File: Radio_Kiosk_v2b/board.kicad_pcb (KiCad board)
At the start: 2 copper layers, 84 x 141 mm, 239 parts, among them J1 USB-C PD in, J11 UART, J12 USB-C, J13 Lid LEDs, J2 DC in 18-26V, PJ-002BH 5.5x2.5, J3 Laptop out 15.6V, PJ-002BH 5.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, J5 RJ45 radio, J6 RJ45 laptop, J8 Fan 12V, J9 SWD, Q1 SI4470EY, Q10 2N7002, Q11 AO3400A, Q12 SI4470EY, Q13 AO4482, Q2 SI4470EY, Q20 AO4482, Q22 PSMN075-100MSEX, Q23 DMP10H400SE, Q24 BSS123, Q25 2N7002, Q30 AO3400A, Q40 AOD4184A, Q41 AOD4184A, Q44 SI4401DDY, Q45 2N7002, Q6 SI4470EY, Q7 SI4470EY, Q8 AOD4185, Q9 2N7002, SW1 RESET, SW2 BOOT0 (DFU), U1 LM74700-Q1, U10 TLV7011, U12 LM74700-Q1, U2 LM74700-Q1, U20 LM3478 54V boost, U21 TPS26600 eFuse, U22 LTC4279, U3 LMR33630 12V, U30 SN74AHCT1G125, U31 SN74AHCT1G125, U4 LM3150 15.75V 4.5A, U40 STM32F072CBT6, U41 INA180A1, U42 INA180A1, U43 MCP6001T-I/OT, U45 TLV7011, U5 LMR33630 5V, U50 CH224A, U51 AP2112K-3.3, U52 USBLC6-2SC6, U6 LM74700-Q1, U7 LM74700-Q1

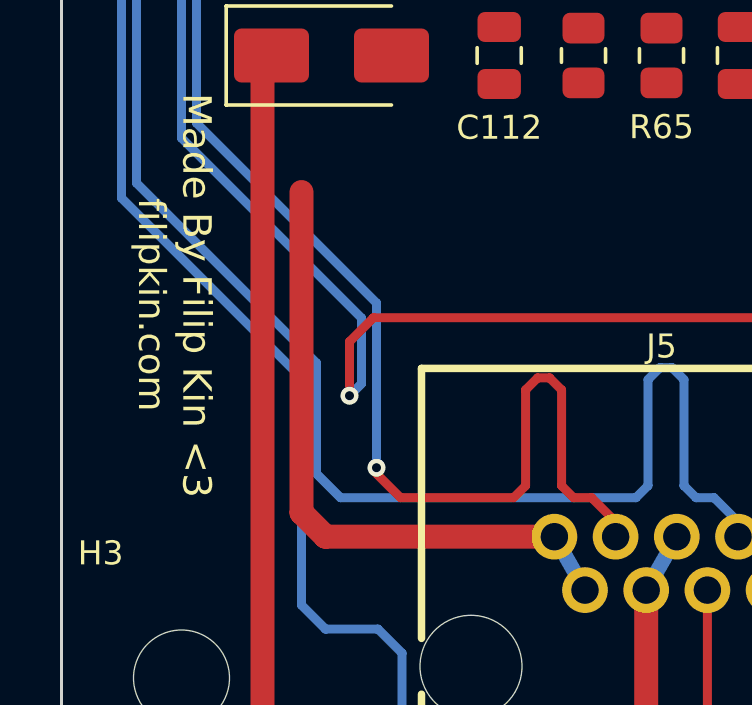
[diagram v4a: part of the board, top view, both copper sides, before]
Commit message: v2b: dead PORT_N lead at J5 removed (it ran to D22, which is now PORT_P to GND)
Co-Authored-By: Claude Opus 5.5 (1M context) <noreply@anthropic.com>
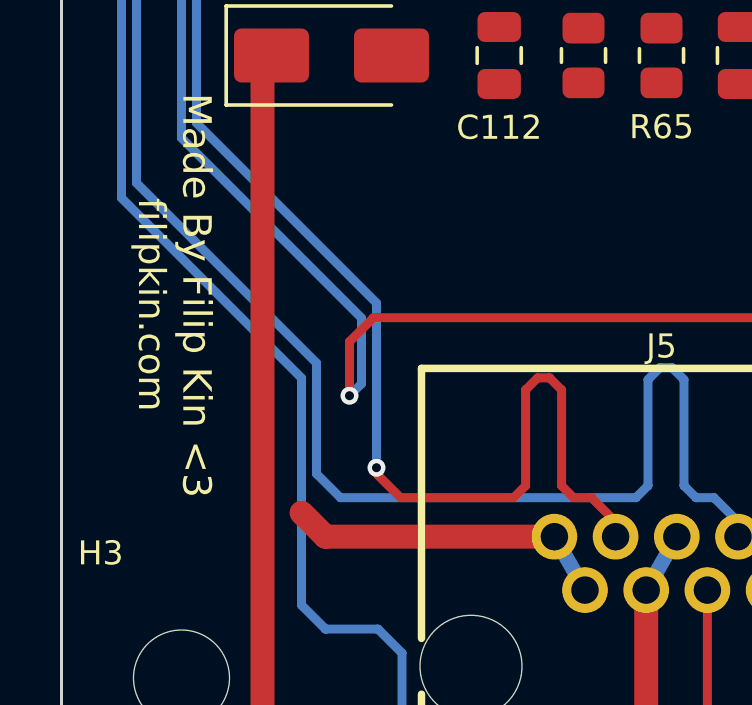
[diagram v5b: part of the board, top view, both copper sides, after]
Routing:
- net PORT_N: track 21.5 -> 10.8 mm
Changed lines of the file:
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@@
-	)
-	(segment
-		(start 8 131.49)
-		(end 8 120.8)
-		(width 0.8)
-		(layer "F.Cu")
-		(net "PORT_N")
 	)
 	(segment

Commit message: v2b: PORT_N and BK_ARM tails left by the earlier removals taken out
Co-Authored-By: Claude Opus 5.5 (1M context) <noreply@anthropic.com>
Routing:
- net PORT_N: track 10.8 -> 2.05 mm
- net BK_ARM: track 1.49 -> 0.00 mm
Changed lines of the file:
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@@
-	)
-	(segment
-		(start 8.8 132.29)
-		(end 8 131.49)
-		(width 0.8)
-		(layer "F.Cu")
-		(net "PORT_N")
-	)
-	(segment
-		(start 16.43 132.29)
-		(end 8.8 132.29)
-		(width 0.8)
-		(layer "F.Cu")
-		(net "PORT_N")
 	)
 	(segment
@@
 		(net "PORT_N")
 	)
-	(segment
-		(start 32.392 53.95)
-		(end 33.444 55.002)
-		(width 0.4)
-		(layer "F.Cu")
-		(net "BK_ARM")
-	)
 	(zone

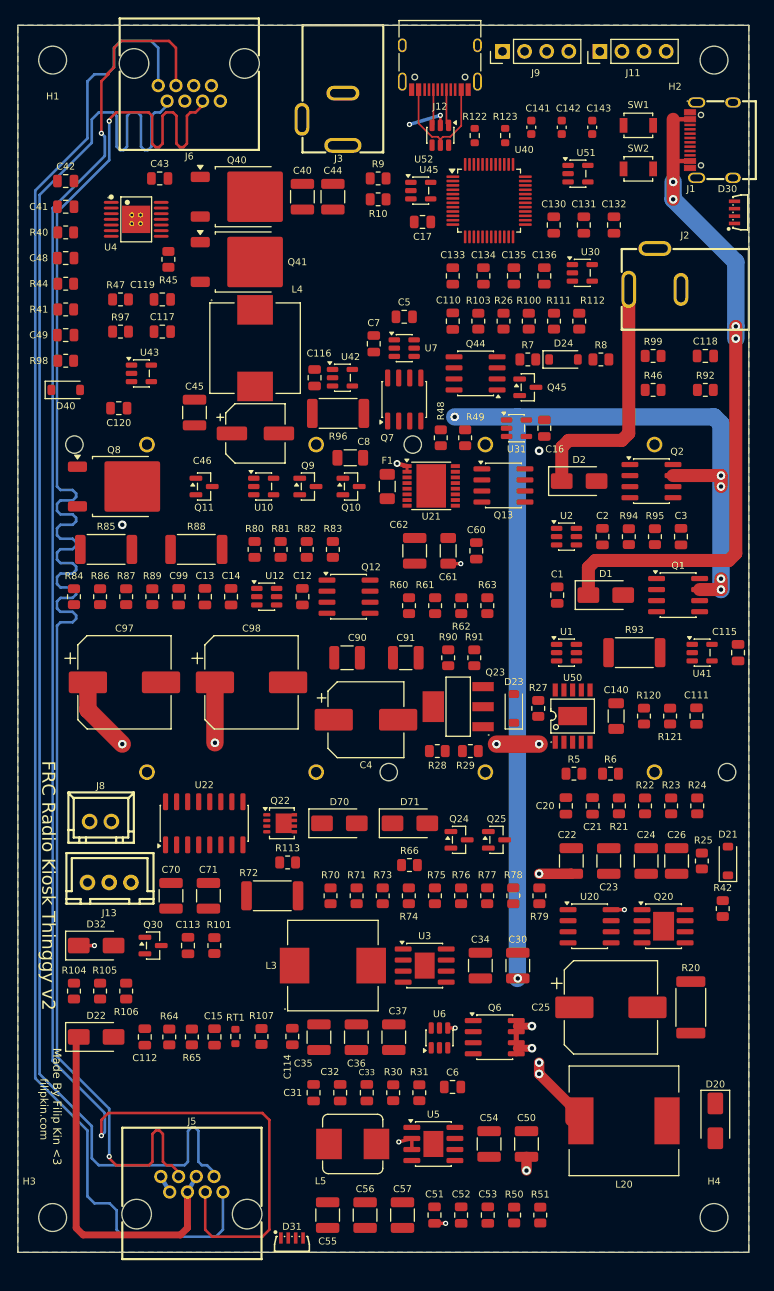
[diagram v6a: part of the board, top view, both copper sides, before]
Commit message: v2b: Filip's hand routing, moved to 1 oz copper
Filip's KiCad routing (1013 segments) taken in, then:
- net classes for 1 oz at ~20 C rise: Heavy 2.0, Wide 1.6, Power 0.8;
  duplicate Power pattern on +15V6_S removed, PORT_SW_G back to Default
- 199 power segments widened to the new class width where they clear
  every other-net pad, track, via, hole (0.25) and the edge; one VIN_USB
  run kept at 1.5 because widening cut D1's ground off
- 50 vias added beside single vias on full-width power runs
  (Heavy/Wide 3, Power 2)
- GND jumpers (via pair + back segment) join three cut-off front GND
  regions (R83, C130, U40.8); R65's region has no room and stays open
- removed: PORT_N run 0.06 mm from ETH_6 at J5, USB_VBUS via crowding
  CC1/CC2 at J12, 5 dangling vias, 1 dangling stub
Ethernet copper identical to the approved routing. DRC errors: only J1's
own 0.10 mm pad gaps.

Co-Authored-By: Claude Opus 5.5 (1M context) <noreply@anthropic.com>
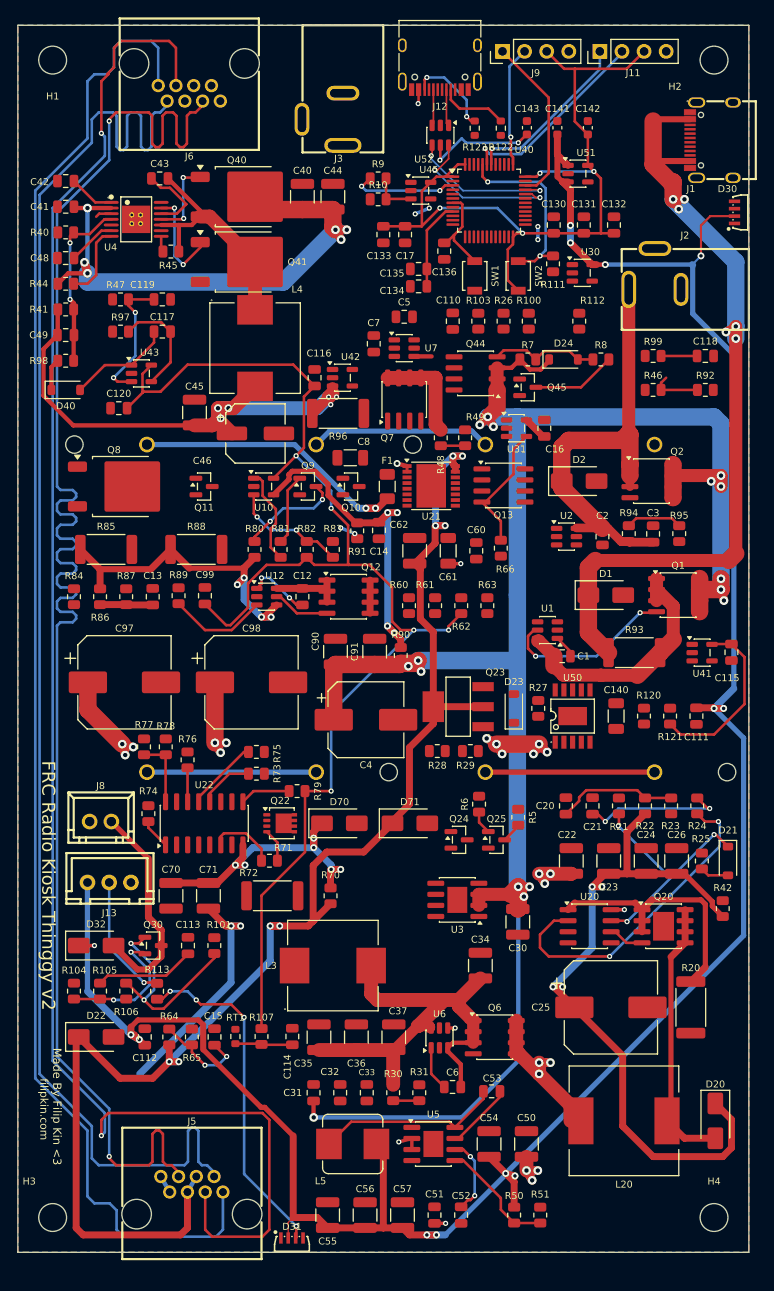
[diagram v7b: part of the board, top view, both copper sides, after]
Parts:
- moved R78 43.4 mm to (17.0, 82.9)
- moved R77 43.0 mm to (14.5, 82.9), turned to -90 degrees
- moved R66 37.9 mm to (55.5, 60.1), turned to -90 degrees
- moved R76 35.1 mm to (19.5, 84.4)
- moved R74 31.4 mm to (15.0, 90.6)
- moved R79 30.3 mm to (32.1, 88.0), turned to 180 degrees
- moved R75 26.3 mm to (27.4, 83.5), turned to 0 degrees
- moved SW1 25.5 mm to (52.5, 28.8), turned to -90 degrees
- moved R113 21.1 mm to (16.0, 111.0), turned to 90 degrees
- moved R73 20.2 mm to (27.4, 86.0), turned to 0 degrees
- moved R91 19.8 mm to (39.0, 58.1), turned to -90 degrees
- moved C14 18.6 mm to (41.5, 58.0), turned to -90 degrees
- moved SW2 18.5 mm to (57.5, 28.8), turned to -90 degrees
- moved R6 15.5 mm to (53.0, 89.5), turned to 90 degrees
- moved C53 14.2 mm to (54.5, 122.5), turned to 180 degrees
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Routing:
- net +5V: track 0.00 -> 279.9 mm, vias 0 -> 12
- net +3V3: track 0.00 -> 262.9 mm, vias 0 -> 9
- net VIN: track 125.0 -> 304.5 mm, vias 6 -> 22
- net PORT_P: track 41.8 -> 165.9 mm, vias 0 -> 8
- net BOOST_OUT: track 0.00 -> 83.1 mm, vias 0 -> 4
- net +15V6_BUCK: track 0.00 -> 66.8 mm, vias 0 -> 6
- net +12V_BUCK: track 0.00 -> 53.4 mm
- net BK_MID: track 0.00 -> 42.5 mm, vias 0 -> 4
- net LED_D2: track 0.00 -> 39.5 mm, vias 0 -> 4
- net VIN_SENSE: track 0.00 -> 38.9 mm, vias 0 -> 4
- net BOOST_COMP: track 0.00 -> 37.4 mm, vias 0 -> 2
- net PSE_AGND: track 0.00 -> 36.0 mm, vias 0 -> 6
- net +12V: track 53.0 -> 86.8 mm, vias 19 -> 28
- net PACK_P: track 0.00 -> 33.3 mm, vias 0 -> 2
- net BOOST_SW: track 0.00 -> 31.5 mm
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
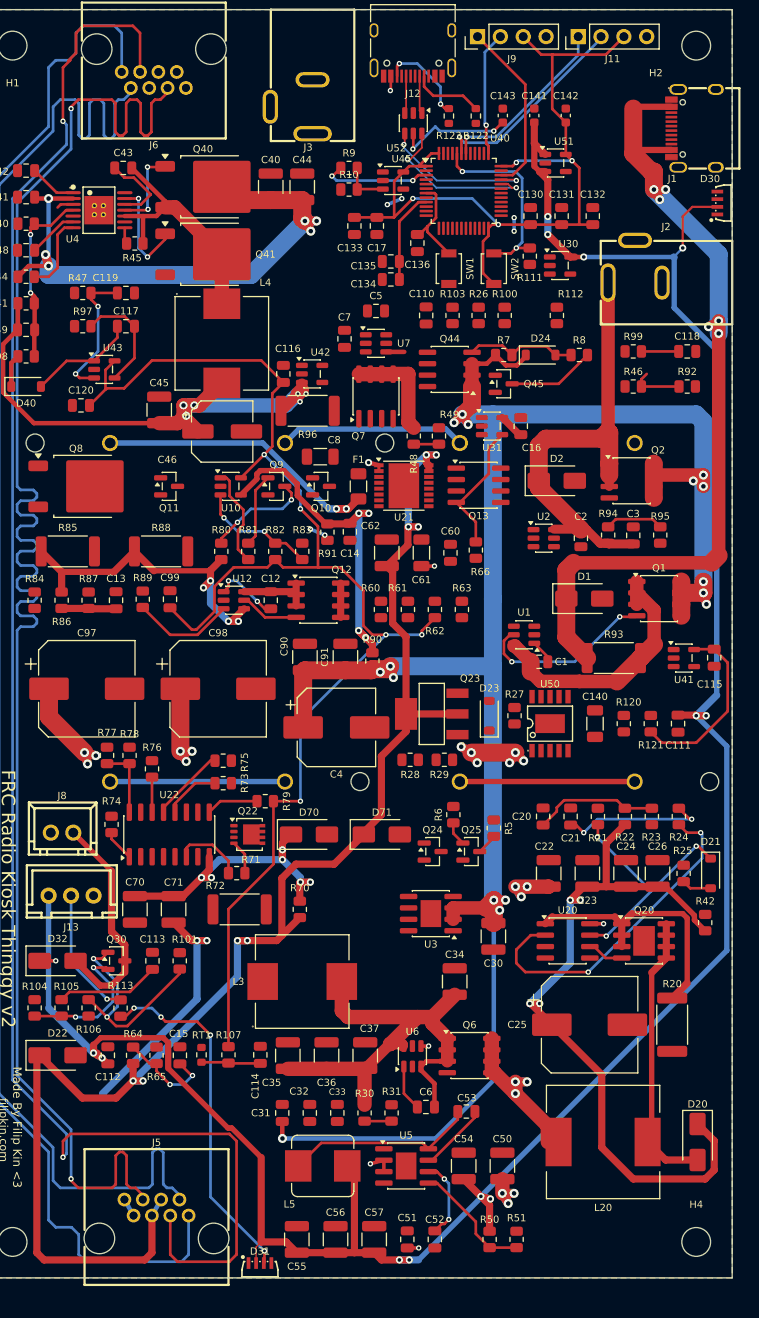
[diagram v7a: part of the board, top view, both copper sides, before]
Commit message: v2b: Filip's routing pass 2 (U3 caps moved in, PORT_N, PD lines, LED chain)
Co-Authored-By: Claude Opus 5.5 (1M context) <noreply@anthropic.com>
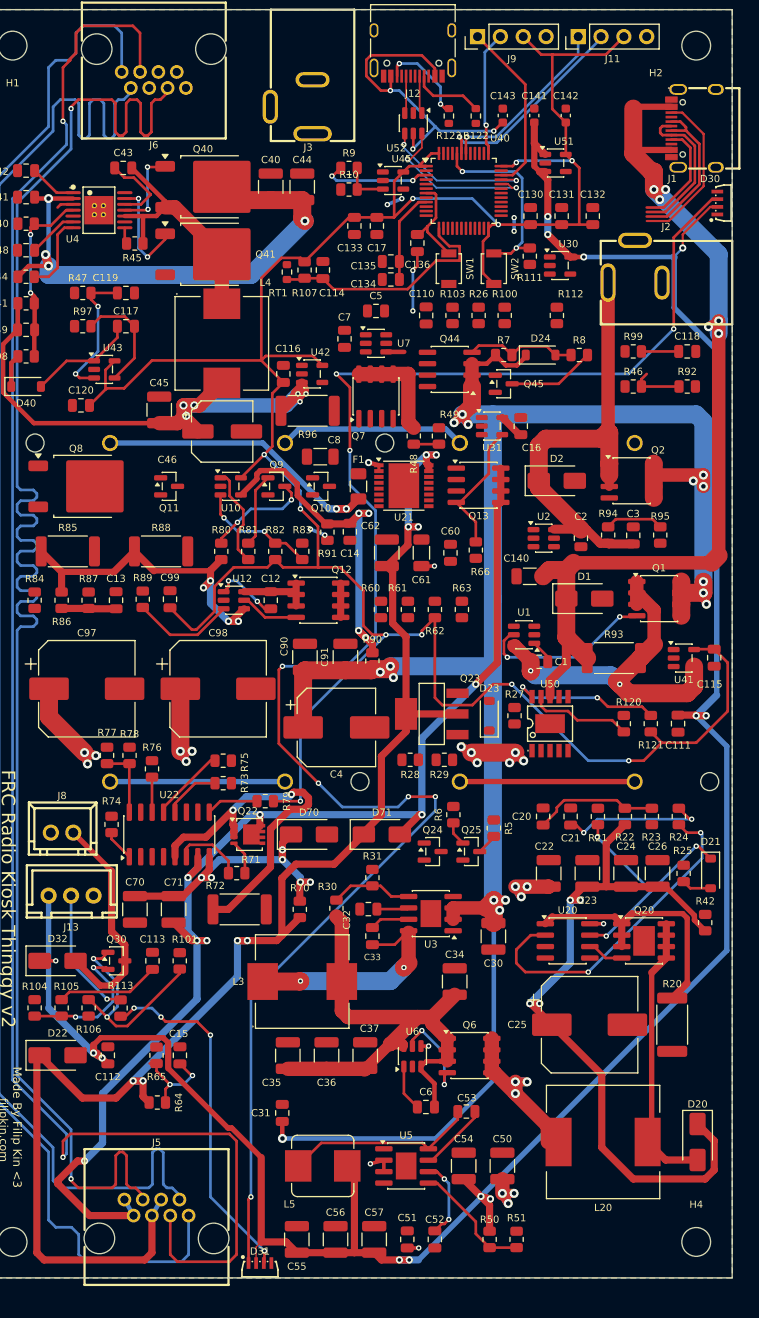
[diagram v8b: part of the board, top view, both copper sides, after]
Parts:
- moved R107 87.7 mm to (36.5, 28.9)
- moved RT1 87.5 mm to (34.5, 29.2)
- moved C114 87.5 mm to (38.5, 28.9)
- moved R31 26.2 mm to (44.0, 96.5)
- moved C32 23.6 mm to (43.5, 100.0), turned to 180 degrees
- moved R30 23.0 mm to (40.0, 99.9), turned to 90 degrees
- moved C33 20.0 mm to (44.0, 103.0), turned to -90 degrees
- moved C140 17.9 mm to (61.5, 63.0), turned to 180 degrees
- moved R64 5.90 mm to (20.1, 121.5), turned to 0 degrees
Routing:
- net LED_D1: track 0.00 -> 189.1 mm, vias 0 -> 8
- net PORT_N: track 29.0 -> 138.7 mm, vias 2 -> 7
- net +3V3: track 262.9 -> 303.3 mm, vias 9 -> 11
- net PSE_SENSE: track 0.00 -> 40.4 mm, vias 0 -> 2
- net U3_SW: track 0.00 -> 25.1 mm, vias 0 -> 2
- net USB_VBUS: track 15.0 -> 36.1 mm
- net TEMP_SENSE: track 6.59 -> 26.3 mm
- net PD_CC2: track 0.00 -> 18.3 mm
- net PD_DP: track 0.00 -> 17.8 mm
- net PD_DM: track 0.00 -> 17.1 mm
- net PD_PG: track 0.00 -> 17.1 mm, vias 0 -> 2
- net PD_CC1: track 0.00 -> 12.2 mm
- net VIN_USBS: track 28.6 -> 40.7 mm, vias 0 -> 2
- net PD_CFG1: track 0.00 -> 11.4 mm
- net U6_GATE: track 0.00 -> 10.6 mm, vias 0 -> 2
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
